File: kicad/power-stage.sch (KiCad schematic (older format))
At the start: 10 parts, among them Q1 KND3508A, U6 PN7006A

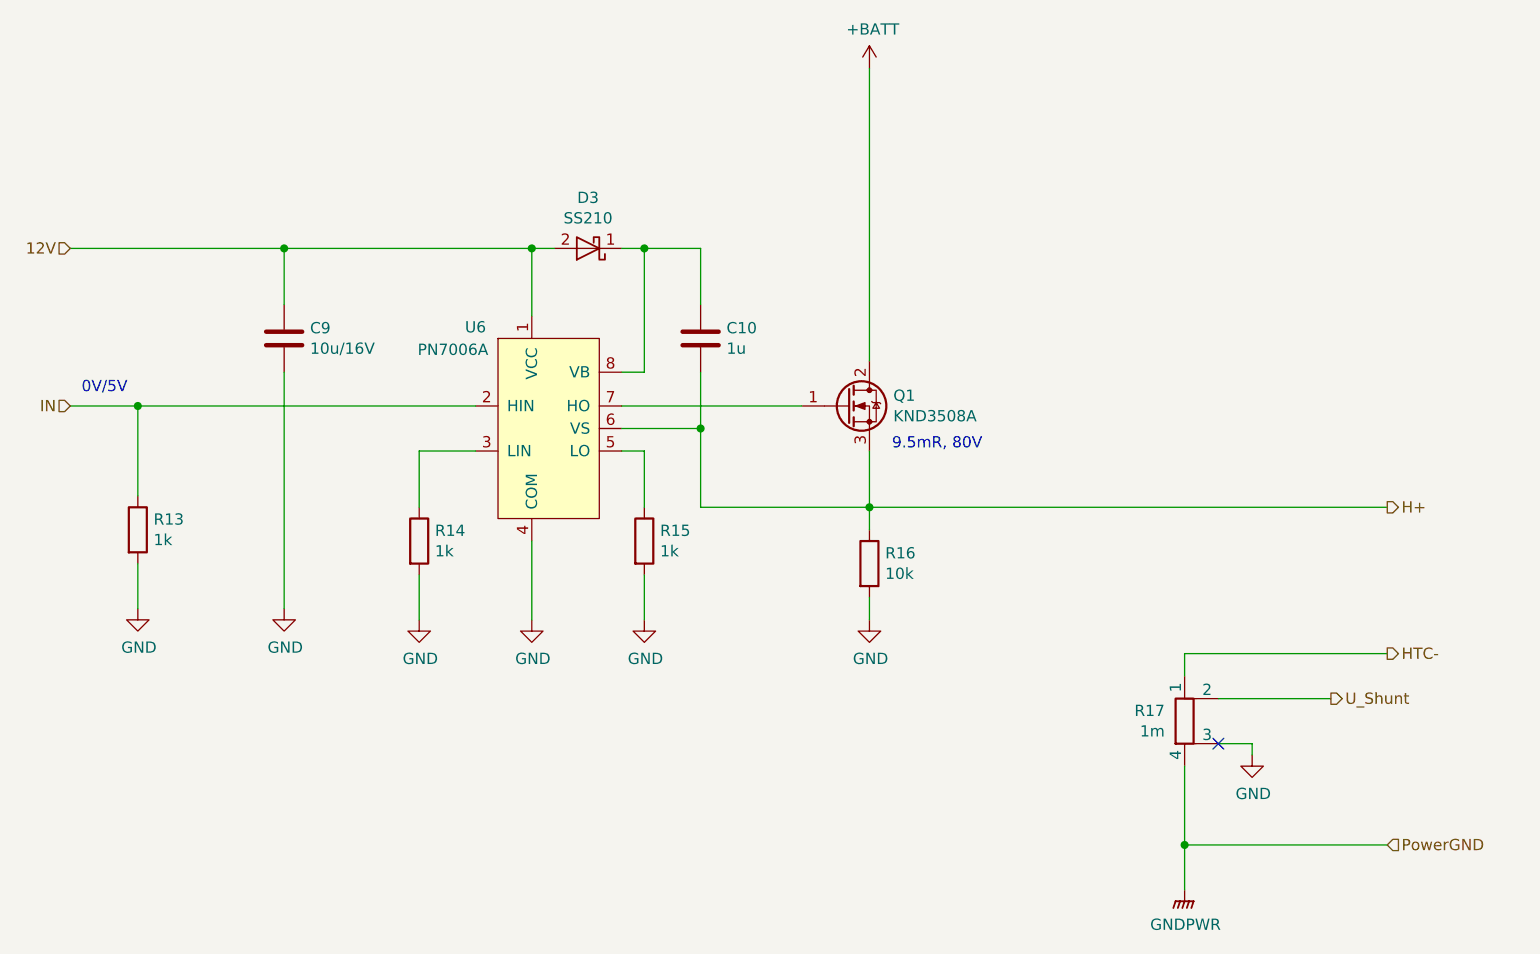
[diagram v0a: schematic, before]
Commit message: BOM ist nun fast fertig
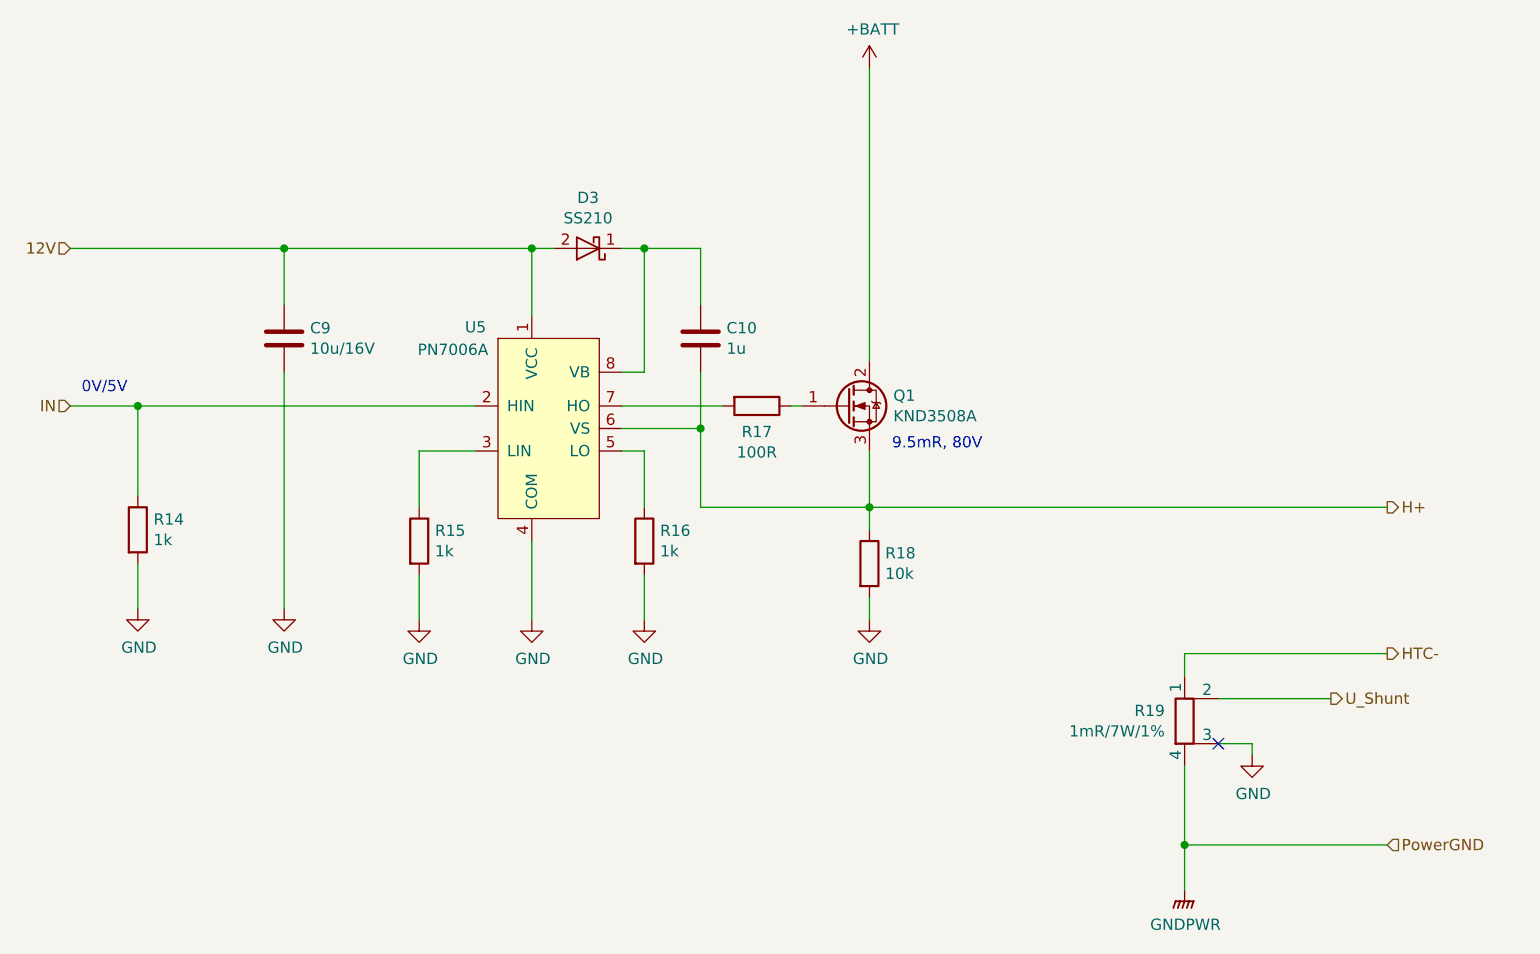
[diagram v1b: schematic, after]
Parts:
- added R17: 100R, Resistor_SMD:R_1206_3216Metric, symbol Device:R
- R14: renamed from R13; PriceEUR (none) -> 0.01
- R15: renamed from R14; PriceEUR (none) -> 0.01
- R16: renamed from R15; PriceEUR (none) -> 0.01
- R18: renamed from R16; PriceEUR (none) -> 0.01
- R19: renamed from R17; value 1m -> 1mR/7W/1%; PriceEUR (none) -> 0.2596; PriceForQty (none) -> 100
- U5: renamed from U6; Notes (none) -> SOP-8 half bridge Driver, 300V, 450mA; PriceEUR (none) -> 0.2188; PriceForQty (none) -> 100; Weblink (none) -> https://lcsc.com/product-detail/Full-bridge-half-bridge-Dri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
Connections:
- net at Q1.1 (G): now also R17.1; no longer U5.7 (HO)
- new net: R17.2, U5.7 (HO)
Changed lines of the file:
@@
 $EndComp
 $Comp
-L Device:R R16
+L Device:R R18
 U 1 1 609FB915
 P 5250 3900
-F 0 "R16" H 5320 3946 50  0000 L CNN
+F 0 "R18" H 5320 3946 50  0000 L CNN
 F 1 "10k" H 5320 3855 50  0000 L CNN
 F 2 "Resistor_SMD:R_1206_3216Metric" V 5180 3900 50  0001 C CNN
 F 3 "~" H 5250 3900 50  0001 C CNN
+F 4 "0.01" H 5250 3900 50  0001 C CNN "PriceEUR"
 	1    5250 3900
 	1    0    0    -1
 $EndComp
 Wire Wire Line
-	4150 3200 4950 3200
+	4150 3200 4600 3200
 Wire Wire Line
 	4150 3300 4500 3300
@@
 	3500 3200 2000 3200
 $Comp
-L Device:R R13
+L Device:R R14
 U 1 1 60A04847
 P 2000 3750
-F 0 "R13" H 2070 3796 50  0000 L CNN
+F 0 "R14" H 2070 3796 50  0000 L CNN
 F 1 "1k" H 2070 3705 50  0000 L CNN
 F 2 "Resistor_SMD:R_1206_3216Metric" V 1930 3750 50  0001 C CNN
 F 3 "~" H 2000 3750 50  0001 C CNN
+F 4 "0.01" H 2000 3750 50  0001 C CNN "PriceEUR"
 	1    2000 3750
 	1    0    0    -1
@@
 IN
 $Comp
-L htl_ics:PN7006A U6
+L htl_ics:PN7006A U5
 U 1 1 609FA816
 P 3750 3300
-F 0 "U6" H 3500 3750 50  0000 C CNN
+F 0 "U5" H 3500 3750 50  0000 C CNN
 F 1 "PN7006A" H 3400 3650 50  0000 C CNN
 F 2 "Package_SO:SOIC-8_3.9x4.9mm_P1.27mm" H 3400 3500 50  0001 C CNN
@@
 F 4 "LCSC" H 3750 3300 50  0001 C CNN "Distributor"
 F 5 "C414194" H 3750 3300 50  0001 C CNN "DistOrderNr"
+F 6 "SOP-8 half bridge Driver, 300V, 450mA" H 3750 3300 50  0001 C CNN "Notes"
+F 7 "0.2188" H 3750 3300 50  0001 C CNN "PriceEUR"
+F 8 "100" H 3750 3300 50  0001 C CNN "PriceForQty"
+F 9 "https://lcsc.com/product-detail/Full-bridge-half-bridge-Driver_Wuxi-Chipown-Micro-electronics-PN7006ASEC-R1_C414194.html" H 3750 3300 50  0001 C CNN "Weblink"
 	1    3750 3300
 	1    0    0    -1
@@
 	3250 3400 3500 3400
 $Comp
-L Device:R R15
+L Device:R R16
 U 1 1 60A08CE0
 P 4250 3800
-F 0 "R15" H 4320 3846 50  0000 L CNN
+F 0 "R16" H 4320 3846 50  0000 L CNN
 F 1 "1k" H 4320 3755 50  0000 L CNN
 F 2 "Resistor_SMD:R_1206_3216Metric" V 4180 3800 50  0001 C CNN
 F 3 "~" H 4250 3800 50  0001 C CNN
+F 4 "0.01" H 4250 3800 50  0001 C CNN "PriceEUR"
 	1    4250 3800
 	1    0    0    -1
@@
 	4250 3400 4250 3650
 $Comp
-L Device:R R14
+L Device:R R15
 U 1 1 60A094FE
 P 3250 3800
-F 0 "R14" H 3320 3846 50  0000 L CNN
+F 0 "R15" H 3320 3846 50  0000 L CNN
 F 1 "1k" H 3320 3755 50  0000 L CNN
 F 2 "Resistor_SMD:R_1206_3216Metric" V 3180 3800 50  0001 C CNN
 F 3 "~" H 3250 3800 50  0001 C CNN
+F 4 "0.01" H 3250 3800 50  0001 C CNN "PriceEUR"
 	1    3250 3800
 	1    0    0    -1
@@
 	4250 3950 4250 4150
 $Comp
-L Device:R_Shunt R17
+L Device:R_Shunt R19
 U 1 1 60A0E53F
 P 6650 4600
-F 0 "R17" H 6562 4646 50  0000 R CNN
-F 1 "1m" H 6562 4555 50  0000 R CNN
+F 0 "R19" H 6562 4646 50  0000 R CNN
+F 1 "1mR/7W/1%" H 6562 4555 50  0000 R CNN
 F 2 "htl_smd:Shunt-15.2x7.6mm" V 6580 4600 50  0001 C CNN
 F 3 "~" H 6650 4600 50  0001 C CNN
 F 4 "LCSC" H 6650 4600 50  0001 C CNN "Distributor"
 F 5 "C481499 " H 6650 4600 50  0001 C CNN "DistOrderNr"
+F 6 "0.2596" H 6650 4600 50  0001 C CNN "PriceEUR"
+F 7 "100" H 6650 4600 50  0001 C CNN "PriceForQty"
 	1    6650 4600
 	1    0    0    -1
@@
 Text Notes 1750 3150 0    50   ~ 0
 0V/5V
+$Comp
+L Device:R R17
+U 1 1 608F2DD6
+P 4750 3200
+F 0 "R17" V 4865 3200 50  0000 C CNN
+F 1 "100R" V 4956 3200 50  0000 C CNN
+F 2 "Resistor_SMD:R_1206_3216Metric" V 4680 3200 50  0001 C CNN
+F 3 "~" H 4750 3200 50  0001 C CNN
+F 4 "0.01" H 4750 3200 50  0001 C CNN "PriceEUR"
+	1    4750 3200
+	0    1    1    0
+$EndComp
+Wire Wire Line
+	4900 3200 4950 3200
 $EndSCHEMATC

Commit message: BOM Fertig, 3D auch fast fertig. Ein paar Footrpints fehlen noch.
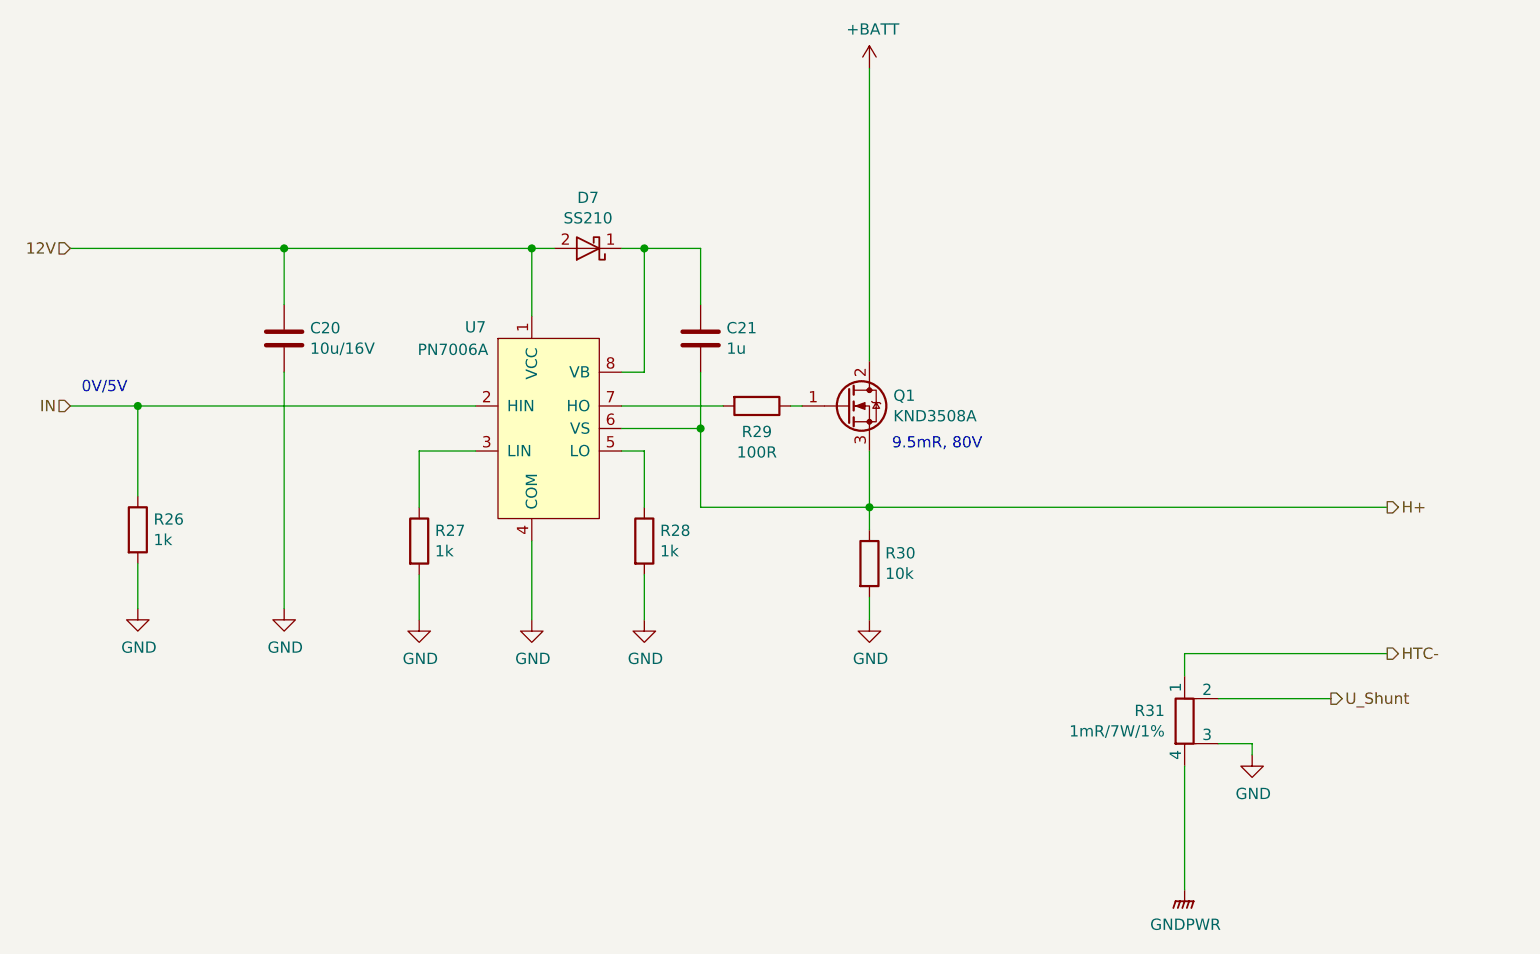
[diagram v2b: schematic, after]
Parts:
- R26: renamed from R14; DistOrderNr (none) -> C104601; Distributor (none) -> LCSC; ManPartNr (none) -> RTT03101JTP; Manufacturer (none) -> RALEC; Notes (none) -> 1kΩ ±5% 0.25W ±100ppm/℃ 1206 Chip Resistor; PriceEUR 0.01 -> 0.0042; PriceForQty (none) -> 50
- R27: renamed from R15; DistOrderNr (none) -> C104601; Distributor (none) -> LCSC; ManPartNr (none) -> RTT03101JTP; Manufacturer (none) -> RALEC; Notes (none) -> 1kΩ ±5% 0.25W ±100ppm/℃ 1206 Chip Resistor; PriceEUR 0.01 -> 0.0042; PriceForQty (none) -> 50
- R28: renamed from R16; DistOrderNr (none) -> C104601; Distributor (none) -> LCSC; ManPartNr (none) -> RTT03101JTP; Manufacturer (none) -> RALEC; Notes (none) -> 1kΩ ±5% 0.25W ±100ppm/℃ 1206 Chip Resistor; PriceEUR 0.01 -> 0.0042; PriceForQty (none) -> 50
- R29: renamed from R17; DistOrderNr (none) -> C113307; Distributor (none) -> LCSC; ManPartNr (none) -> RC1206JR-07100RL; Manufacturer (none) -> YAGEO; Notes (none) -> 100Ω ±5% 0.25W ±100ppm/℃ 1206 Chip Resistor; PriceEUR 0.01 -> 0.0037; PriceForQty (none) -> 500
- R30: renamed from R18; DistOrderNr (none) -> C118075; Distributor (none) -> LCSC
- renumbered C9 to C20, C10 to C21, D3 to D7, R19 to R31, U5 to U7
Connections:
- no-connect marks 1 -> 0
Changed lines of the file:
@@
 $Descr A4 11693 8268
 encoding utf-8
-Sheet 4 8
+Sheet 5 10
 Title "JBC-Miniregler"
 Date "2021-05-02"
@@
 $EndComp
 $Comp
-L Device:R R18
+L Device:R R30
 U 1 1 609FB915
 P 5250 3900
-F 0 "R18" H 5320 3946 50  0000 L CNN
+F 0 "R30" H 5320 3946 50  0000 L CNN
 F 1 "10k" H 5320 3855 50  0000 L CNN
 F 2 "Resistor_SMD:R_1206_3216Metric" V 5180 3900 50  0001 C CNN
 F 3 "~" H 5250 3900 50  0001 C CNN
 F 4 "0.01" H 5250 3900 50  0001 C CNN "PriceEUR"
+F 5 "C118075" H 5250 3900 50  0001 C CNN "DistOrderNr"
+F 6 "LCSC" H 5250 3900 50  0001 C CNN "Distributor"
 	1    5250 3900
 	1    0    0    -1
@@
 	5250 3650 5250 3750
 $Comp
-L Device:C C10
+L Device:C C21
 U 1 1 609FBE75
 P 4500 2900
-F 0 "C10" H 4615 2946 50  0000 L CNN
+F 0 "C21" H 4615 2946 50  0000 L CNN
 F 1 "1u" H 4615 2855 50  0000 L CNN
 F 2 "Capacitor_SMD:C_1206_3216Metric" H 4538 2750 50  0001 C CNN
@@
 Connection ~ 4250 2500
 $Comp
-L htl_semiconductors:D_Schottky D3
+L htl_semiconductors:D_Schottky D7
 U 1 1 60A01F4E
 P 4000 2500
-F 0 "D3" H 4000 2275 50  0000 C CNN
+F 0 "D7" H 4000 2275 50  0000 C CNN
 F 1 "SS210" H 4000 2366 50  0000 C CNN
 F 2 "Diode_SMD:D_SMA" H 4000 2500 50  0001 C CNN
@@
 $EndComp
 $Comp
-L power:+BATT #PWR020
+L power:+BATT #PWR042
 U 1 1 60A0291F
 P 5250 1700
-F 0 "#PWR020" H 5250 1550 50  0001 C CNN
+F 0 "#PWR042" H 5250 1550 50  0001 C CNN
 F 1 "+BATT" H 5265 1873 50  0000 C CNN
 F 2 "" H 5250 1700 50  0001 C CNN
@@
 Connection ~ 3750 2500
 $Comp
-L Device:C C9
+L Device:C C20
 U 1 1 60A033E2
 P 2650 2900
-F 0 "C9" H 2765 2946 50  0000 L CNN
+F 0 "C20" H 2765 2946 50  0000 L CNN
 F 1 "10u/16V" H 2765 2855 50  0000 L CNN
 F 2 "Capacitor_SMD:C_1206_3216Metric" H 2688 2750 50  0001 C CNN
@@
 	2650 2500 3750 2500
 $Comp
-L power:GND #PWR016
+L power:GND #PWR038
 U 1 1 60A03E97
 P 2650 4100
-F 0 "#PWR016" H 2650 3850 50  0001 C CNN
+F 0 "#PWR038" H 2650 3850 50  0001 C CNN
 F 1 "GND" H 2655 3927 50  0000 C CNN
 F 2 "" H 2650 4100 50  0001 C CNN
@@
 	3500 3200 2000 3200
 $Comp
-L Device:R R14
+L Device:R R26
 U 1 1 60A04847
 P 2000 3750
-F 0 "R14" H 2070 3796 50  0000 L CNN
+F 0 "R26" H 2070 3796 50  0000 L CNN
 F 1 "1k" H 2070 3705 50  0000 L CNN
 F 2 "Resistor_SMD:R_1206_3216Metric" V 1930 3750 50  0001 C CNN
 F 3 "~" H 2000 3750 50  0001 C CNN
-F 4 "0.01" H 2000 3750 50  0001 C CNN "PriceEUR"
+F 4 "0.0042" H 2000 3750 50  0001 C CNN "PriceEUR"
+F 5 "C104601" H 2000 3750 50  0001 C CNN "DistOrderNr"
+F 6 "LCSC" H 2000 3750 50  0001 C CNN "Distributor"
+F 7 "RTT03101JTP" H 2000 3750 50  0001 C CNN "ManPartNr"
+F 8 "RALEC" H 2000 3750 50  0001 C CNN "Manufacturer"
+F 9 "1kΩ ±5% 0.25W ±100ppm/℃ 1206 Chip Resistor" H 2000 3750 50  0001 C CNN "Notes"
+F 10 "50" H 2000 3750 50  0001 C CNN "PriceForQty"
 	1    2000 3750
 	1    0    0    -1
@@
 	2000 3200 1700 3200
 $Comp
-L power:GND #PWR015
+L power:GND #PWR037
 U 1 1 60A04F8A
 P 2000 4100
-F 0 "#PWR015" H 2000 3850 50  0001 C CNN
+F 0 "#PWR037" H 2000 3850 50  0001 C CNN
 F 1 "GND" H 2005 3927 50  0000 C CNN
 F 2 "" H 2000 4100 50  0001 C CNN
@@
 	2000 4100 2000 3900
 $Comp
-L power:GND #PWR021
+L power:GND #PWR043
 U 1 1 60A05E12
 P 5250 4150
-F 0 "#PWR021" H 5250 3900 50  0001 C CNN
+F 0 "#PWR043" H 5250 3900 50  0001 C CNN
 F 1 "GND" H 5255 3977 50  0000 C CNN
 F 2 "" H 5250 4150 50  0001 C CNN
@@
 	5250 4150 5250 4050
 $Comp
-L power:GND #PWR018
+L power:GND #PWR040
 U 1 1 60A06F12
 P 3750 4150
-F 0 "#PWR018" H 3750 3900 50  0001 C CNN
+F 0 "#PWR040" H 3750 3900 50  0001 C CNN
 F 1 "GND" H 3755 3977 50  0000 C CNN
 F 2 "" H 3750 4150 50  0001 C CNN
@@
 IN
 $Comp
-L htl_ics:PN7006A U5
+L htl_ics:PN7006A U7
 U 1 1 609FA816
 P 3750 3300
-F 0 "U5" H 3500 3750 50  0000 C CNN
+F 0 "U7" H 3500 3750 50  0000 C CNN
 F 1 "PN7006A" H 3400 3650 50  0000 C CNN
 F 2 "Package_SO:SOIC-8_3.9x4.9mm_P1.27mm" H 3400 3500 50  0001 C CNN
@@
 	3250 3400 3500 3400
 $Comp
-L Device:R R16
+L Device:R R28
 U 1 1 60A08CE0
 P 4250 3800
-F 0 "R16" H 4320 3846 50  0000 L CNN
+F 0 "R28" H 4320 3846 50  0000 L CNN
 F 1 "1k" H 4320 3755 50  0000 L CNN
 F 2 "Resistor_SMD:R_1206_3216Metric" V 4180 3800 50  0001 C CNN
 F 3 "~" H 4250 3800 50  0001 C CNN
-F 4 "0.01" H 4250 3800 50  0001 C CNN "PriceEUR"
+F 4 "0.0042" H 4250 3800 50  0001 C CNN "PriceEUR"
+F 5 "C104601" H 4250 3800 50  0001 C CNN "DistOrderNr"
+F 6 "LCSC" H 4250 3800 50  0001 C CNN "Distributor"
+F 7 "RTT03101JTP" H 4250 3800 50  0001 C CNN "ManPartNr"
+F 8 "RALEC" H 4250 3800 50  0001 C CNN "Manufacturer"
+F 9 "1kΩ ±5% 0.25W ±100ppm/℃ 1206 Chip Resistor" H 4250 3800 50  0001 C CNN "Notes"
+F 10 "50" H 4250 3800 50  0001 C CNN "PriceForQty"
 	1    4250 3800
 	1    0    0    -1
@@
 	4250 3400 4250 3650
 $Comp
-L Device:R R15
+L Device:R R27
 U 1 1 60A094FE
 P 3250 3800
-F 0 "R15" H 3320 3846 50  0000 L CNN
+F 0 "R27" H 3320 3846 50  0000 L CNN
 F 1 "1k" H 3320 3755 50  0000 L CNN
 F 2 "Resistor_SMD:R_1206_3216Metric" V 3180 3800 50  0001 C CNN
 F 3 "~" H 3250 3800 50  0001 C CNN
-F 4 "0.01" H 3250 3800 50  0001 C CNN "PriceEUR"
+F 4 "0.0042" H 3250 3800 50  0001 C CNN "PriceEUR"
+F 5 "C104601" H 3250 3800 50  0001 C CNN "DistOrderNr"
+F 6 "LCSC" H 3250 3800 50  0001 C CNN "Distributor"
+F 7 "RTT03101JTP" H 3250 3800 50  0001 C CNN "ManPartNr"
+F 8 "RALEC" H 3250 3800 50  0001 C CNN "Manufacturer"
+F 9 "1kΩ ±5% 0.25W ±100ppm/℃ 1206 Chip Resistor" H 3250 3800 50  0001 C CNN "Notes"
+F 10 "50" H 3250 3800 50  0001 C CNN "PriceForQty"
 	1    3250 3800
 	1    0    0    -1
 $EndComp
 $Comp
-L power:GND #PWR017
+L power:GND #PWR039
 U 1 1 60A09861
 P 3250 4150
-F 0 "#PWR017" H 3250 3900 50  0001 C CNN
+F 0 "#PWR039" H 3250 3900 50  0001 C CNN
 F 1 "GND" H 3255 3977 50  0000 C CNN
 F 2 "" H 3250 4150 50  0001 C CNN
@@
 	3250 4150 3250 3950
 $Comp
-L power:GND #PWR019
+L power:GND #PWR041
 U 1 1 60A0A16F
 P 4250 4150
-F 0 "#PWR019" H 4250 3900 50  0001 C CNN
+F 0 "#PWR041" H 4250 3900 50  0001 C CNN
 F 1 "GND" H 4255 3977 50  0000 C CNN
 F 2 "" H 4250 4150 50  0001 C CNN
@@
 	4250 3950 4250 4150
 $Comp
-L Device:R_Shunt R19
+L Device:R_Shunt R31
 U 1 1 60A0E53F
 P 6650 4600
-F 0 "R19" H 6562 4646 50  0000 R CNN
+F 0 "R31" H 6562 4646 50  0000 R CNN
 F 1 "1mR/7W/1%" H 6562 4555 50  0000 R CNN
 F 2 "htl_smd:Shunt-15.2x7.6mm" V 6580 4600 50  0001 C CNN
@@
 	5250 3650 7550 3650
 $Comp
-L power:GNDPWR #PWR022
+L power:GNDPWR #PWR044
 U 1 1 60A12125
 P 6650 5350
-F 0 "#PWR022" H 6650 5150 50  0001 C CNN
+F 0 "#PWR044" H 6650 5150 50  0001 C CNN
 F 1 "GNDPWR" H 6654 5196 50  0000 C CNN
 F 2 "" H 6650 5300 50  0001 C CNN
@@
 $EndComp
 $Comp
-L power:GND #PWR023
+L power:GND #PWR045
 U 1 1 60A13263
 P 6950 4750
-F 0 "#PWR023" H 6950 4500 50  0001 C CNN
+F 0 "#PWR045" H 6950 4500 50  0001 C CNN
 F 1 "GND" H 6955 4577 50  0000 C CNN
 F 2 "" H 6950 4750 50  0001 C CNN
@@
 	1    0    0    -1
 $EndComp
-NoConn ~ 6800 4700
 Wire Wire Line
 	6800 4500 7300 4500
@@
 Text Notes 5350 3400 0    50   ~ 0
 9.5mR, 80V
-Text HLabel 7550 5150 2    50   Input ~ 0
-PowerGND
-Wire Wire Line
-	6650 4800 6650 5150
-Connection ~ 6650 5150
-Wire Wire Line
-	6650 5150 6650 5350
-Wire Wire Line
-	6650 5150 7550 5150
 Wire Wire Line
 	6800 4700 6950 4700
@@
 0V/5V
 $Comp
-L Device:R R17
+L Device:R R29
 U 1 1 608F2DD6
 P 4750 3200
-F 0 "R17" V 4865 3200 50  0000 C CNN
+F 0 "R29" V 4865 3200 50  0000 C CNN
 F 1 "100R" V 4956 3200 50  0000 C CNN
 F 2 "Resistor_SMD:R_1206_3216Metric" V 4680 3200 50  0001 C CNN
 F 3 "~" H 4750 3200 50  0001 C CNN
-F 4 "0.01" H 4750 3200 50  0001 C CNN "PriceEUR"
+F 4 "0.0037" H 4750 3200 50  0001 C CNN "PriceEUR"
+F 5 "C113307" H 4750 3200 50  0001 C CNN "DistOrderNr"
+F 6 "LCSC" H 4750 3200 50  0001 C CNN "Distributor"
+F 7 "RC1206JR-07100RL" H 4750 3200 50  0001 C CNN "ManPartNr"
+F 8 "YAGEO" H 4750 3200 50  0001 C CNN "Manufacturer"
+F 9 "100Ω ±5% 0.25W ±100ppm/℃ 1206 Chip Resistor" H 4750 3200 50  0001 C CNN "Notes"
+F 10 "500" H 4750 3200 50  0001 C CNN "PriceForQty"
 	1    4750 3200
 	0    1    1    0
@@
 Wire Wire Line
 	4900 3200 4950 3200
+Wire Wire Line
+	6650 4800 6650 5350
 $EndSCHEMATC

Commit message: kleinere Updates im Schaltplan
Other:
- note added: "Integrierte\n"Grid Tie"-Verbindung\nzu Deutsch: Massesternpunkt."
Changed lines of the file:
@@
 Wire Wire Line
 	6650 4800 6650 5350
+Text Notes 6800 5300 0    50   ~ 0
+Integrierte\n"Grid Tie"-Verbindung\nzu Deutsch: Massesternpunkt.
 $EndSCHEMATC
